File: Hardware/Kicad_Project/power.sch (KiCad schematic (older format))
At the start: 3 parts

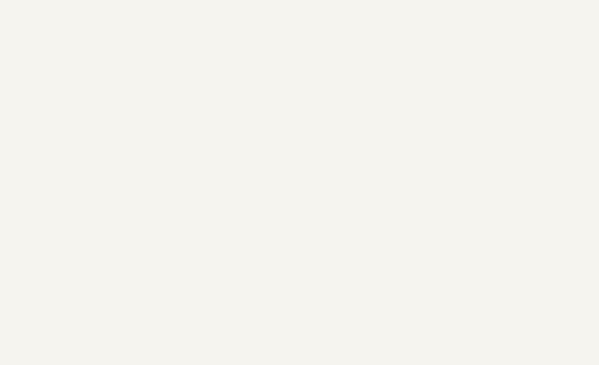
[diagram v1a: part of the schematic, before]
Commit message: [HARWARE] Add AX12 power
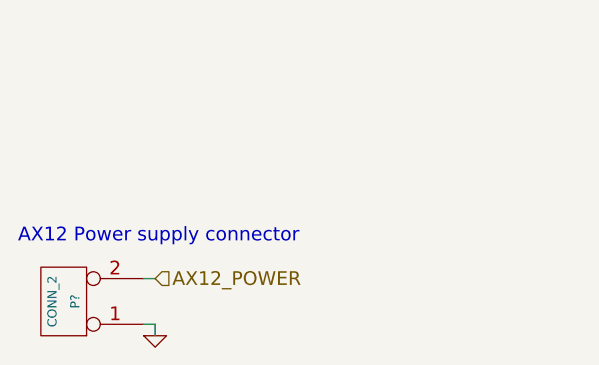
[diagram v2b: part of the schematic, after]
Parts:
- added P?: CONN_2, symbol CONN_2
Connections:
- net GND: now also P?.1 (P1)
- new net AX12_POWER: P?.2 (PM)
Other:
- note added: "AX12 Power supply connector"
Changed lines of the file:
@@
-EESchema Schematic File Version 2  date dim. 06 oct. 2013 19:04:08 CEST
+EESchema Schematic File Version 2  date dim. 06 oct. 2013 19:08:01 CEST
 LIBS:power
 LIBS:device
@@
 Comment4 ""
 $EndDescr
-Text Notes 3900 2500 0    60   ~ 0
-3.3V regulator
+Text Notes 2550 4650 0    60   ~ 0
+AX12 Power supply connector
+Wire Wire Line
+	3150 4800 3100 4800
 Wire Wire Line
 	3500 2850 3500 2800
@@
 	3500 3300 3500 3250
 Connection ~ 4100 3300
+Wire Wire Line
+	3150 5050 3150 5000
+Wire Wire Line
+	3150 5000 3100 5000
+Text HLabel 3150 4800 2    60   Input ~ 0
+AX12_POWER
+$Comp
+L GND #PWR?
+U 1 1 525198A8
+P 3150 5050
+F 0 "#PWR?" H 3150 5050 30  0001 C CNN
+F 1 "GND" H 3150 4980 30  0001 C CNN
+	1    3150 5050
+	1    0    0    -1
+$EndComp
+$Comp
+L CONN_2 P?
+U 1 1 5251989A
+P 2750 4900
+F 0 "P?" V 2700 4900 40  0000 C CNN
+F 1 "CONN_2" V 2800 4900 40  0000 C CNN
+	1    2750 4900
+	-1   0    0    1
+$EndComp
+Text Notes 3900 2500 0    60   ~ 0
+3.3V regulator
 $Comp
 L C C?

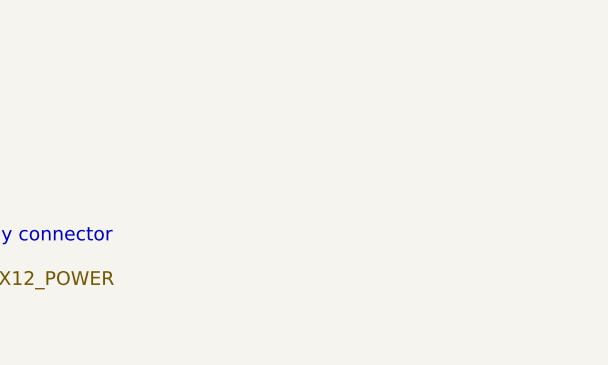
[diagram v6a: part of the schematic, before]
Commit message: [HARDWARE] Add ADC and GP2 interfaces
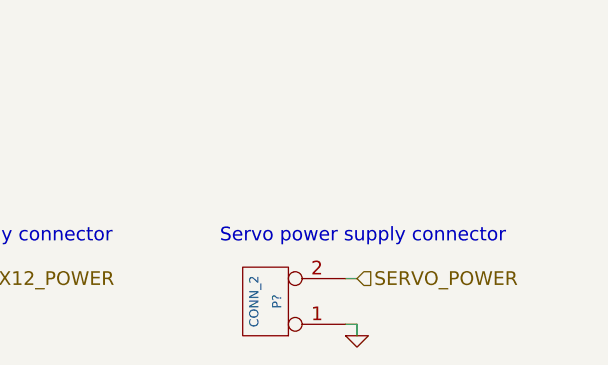
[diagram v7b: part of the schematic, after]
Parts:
- added P?: CONN_2, symbol CONN_2
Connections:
- net GND: now also P?.1 (P1)
- new net SERVO_POWER: P?.2 (PM)
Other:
- note added: "Servo power supply connector"
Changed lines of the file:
@@
-EESchema Schematic File Version 2  date dim. 06 oct. 2013 19:54:20 CEST
+EESchema Schematic File Version 2  date mar. 08 oct. 2013 19:30:07 CEST
 LIBS:power
 LIBS:device
@@
 Sheet 2 5
 Title ""
-Date "6 oct 2013"
+Date "8 oct 2013"
 Rev ""
 Comp ""
@@
 Comment4 ""
 $EndDescr
+$Comp
+L CONN_2 P?
+U 1 1 52543C3C
+P 4450 4900
+F 0 "P?" V 4400 4900 40  0000 C CNN
+F 1 "CONN_2" V 4500 4900 40  0000 C CNN
+	1    4450 4900
+	-1   0    0    1
+$EndComp
+$Comp
+L GND #PWR?
+U 1 1 52543C3B
+P 4850 5050
+F 0 "#PWR?" H 4850 5050 30  0001 C CNN
+F 1 "GND" H 4850 4980 30  0001 C CNN
+	1    4850 5050
+	1    0    0    -1
+$EndComp
+Text HLabel 4850 4800 2    60   Input ~ 0
+SERVO_POWER
+Wire Wire Line
+	4850 5000 4800 5000
+Wire Wire Line
+	4850 5050 4850 5000
+Wire Wire Line
+	4850 4800 4800 4800
+Text Notes 4250 4650 0    60   ~ 0
+Servo power supply connector
 Text Notes 2550 4650 0    60   ~ 0
 AX12 Power supply connector
